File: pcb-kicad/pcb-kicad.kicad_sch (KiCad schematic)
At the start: 17 parts, among them J1 Barrel_Jack_Switch, J2 Screw_Terminal_01x02, J3 Conn_01x03_Pin, J4 Conn_01x02_Pin, J5 Screw_Terminal_01x02, J6 Conn_01x02_Pin, J7 Conn_01x03_Pin, U1 LM317_TO-220, U2 LM7805_TO220

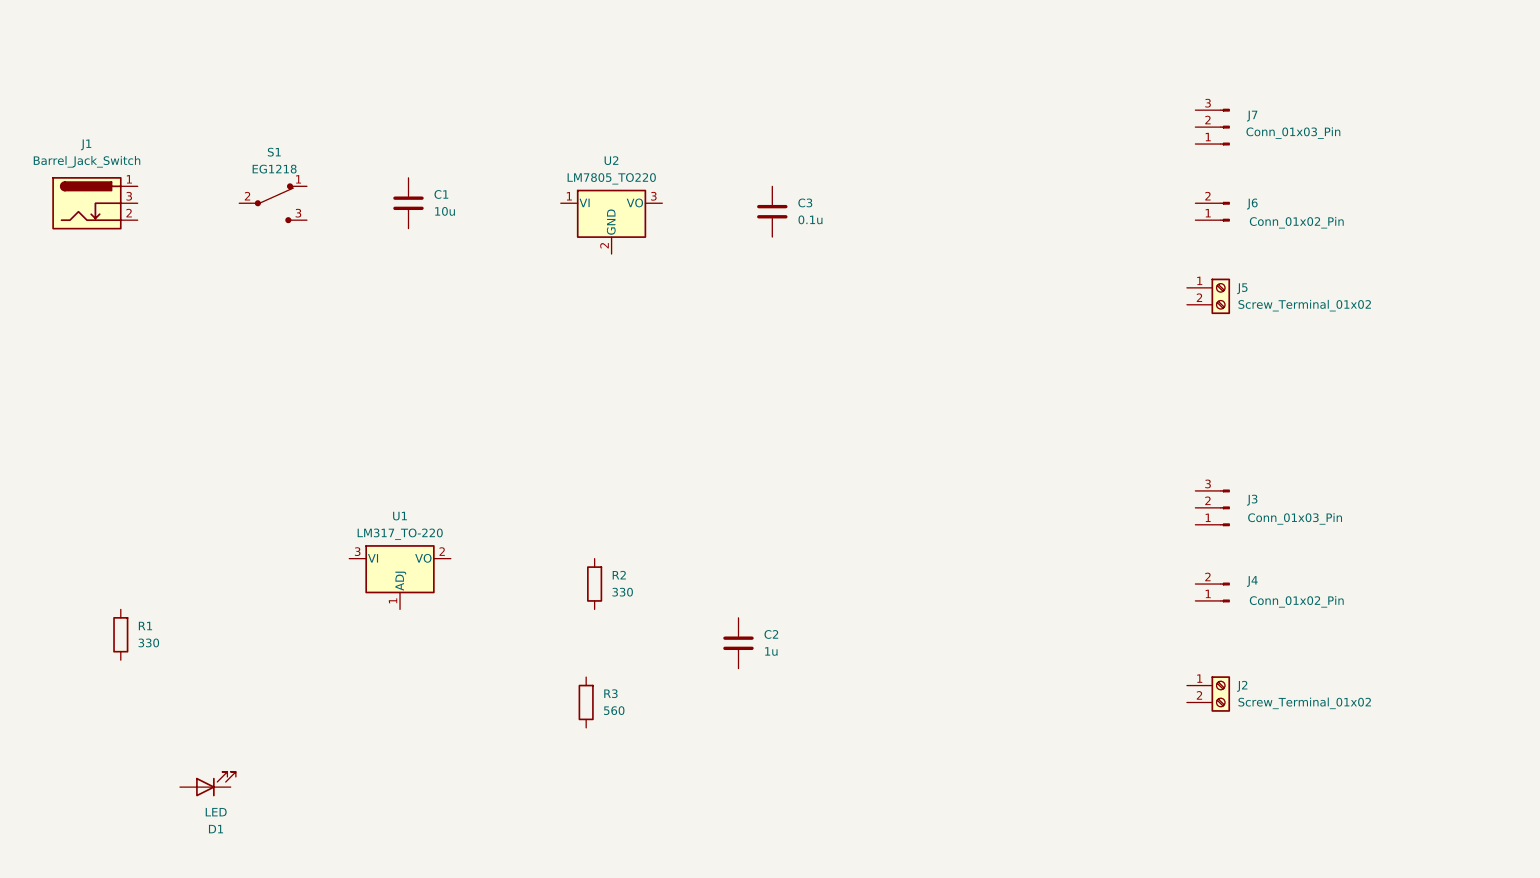
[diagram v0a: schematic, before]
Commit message: Schematic completed. Connections, nets, net classes, comments added.
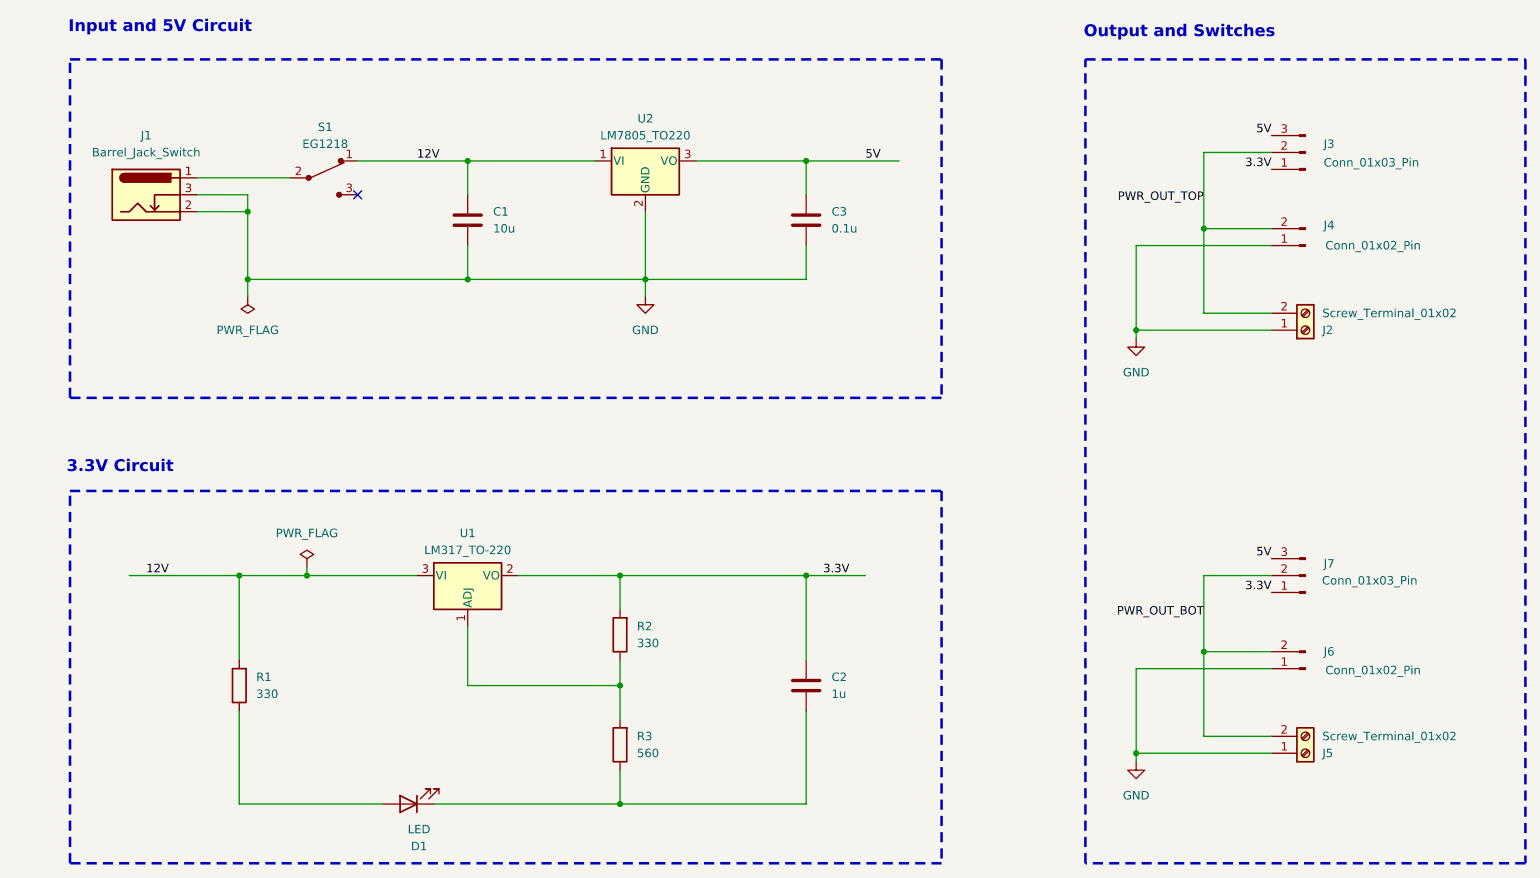
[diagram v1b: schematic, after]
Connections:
- net at R2.1: now also R3.2, U1.1 (ADJ)
- net 3.3V: now reaches R2.2
- net 3.3V: now also C2.1, J3.1 (Pin_1), J7.1 (Pin_1), U1.2 (VO)
- net GND: now reaches J4.1 (Pin_1)
- net GND: now also C1.2, C3.2, J1.2, J1.3, J2.1 (Pin_1), J5.1 (Pin_1), J6.1 (Pin_1), U2.2 (GND)
- net PWR_OUT_TOP: now reaches J4.2 (Pin_2)
- net PWR_OUT_TOP: now also J2.2 (Pin_2), J3.2 (Pin_2)
- net 12V: now reaches C1.1
- net 12V: now also R1.2, S1.1, U1.3 (VI), U2.1 (VI)
- net 5V: now reaches U2.3 (VO)
- net 5V: now also C3.1, J3.3 (Pin_3), J7.3 (Pin_3)
- net at C2.2: now also D1.1 (K), R3.1
- net at J1.1: now also S1.2
- net PWR_OUT_BOT: now reaches J7.2 (Pin_2)
- net PWR_OUT_BOT: now also J5.2 (Pin_2), J6.2 (Pin_2)
- net at R1.1: now also D1.2 (A)
- no-connect marks 0 -> 1
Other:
- note added: "3.3V Circuit"
- note added: "Input and 5V Circuit"
- note added: "Output and Switches"
- company: Nelson Rodriguez - @Lendzeg -> Nelson Rodriguez - Lendzeg
- moved on the sheet: C1, C2, C3, D1, J1, J2, J3, J4, J5, J6, J7, R1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
